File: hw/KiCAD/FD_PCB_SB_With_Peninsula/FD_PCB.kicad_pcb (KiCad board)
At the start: 2 copper layers, 251.3 x 143.9 mm, 169 parts, among them J1 Barrel_Jack_Switch, J10 Conn_01x02, J11 Conn_01x02, J12 Conn_01x02, J13 Conn_02x10_Odd_Even, J14 MQ-4 Gas Sensor, J15 MQ-7 Gas Sensor, J16 MQ-138 Gas Sensor, J17 KY-026 Flame Sensor, J18 Conn_01x10, J19 Conn_01x05, J2 Conn_02x12_Odd_Even, J20 HDC3022, J21 Conn_01x08, J22 MiCS-6814, J23 Conn_01x02, J24 Conn_01x02, J25 Conn_01x02, J3 Conn_02x12_Odd_Even, J4 Conn_02x20_Odd_Even, J5 Conn_02x10_Odd_Even, J6 Conn_01x07, J7 Conn_01x02, J8 Conn_01x08, J9 Conn_01x16, M1 Motor_Servo, M2 Motor_Servo, SW1 SW_Push, SW2 SW_Push, SW3 SW_Push, U1 ADS1115IDGS, U2 OPA2350, U3 OPA2350, U4 ADS1115IDGS

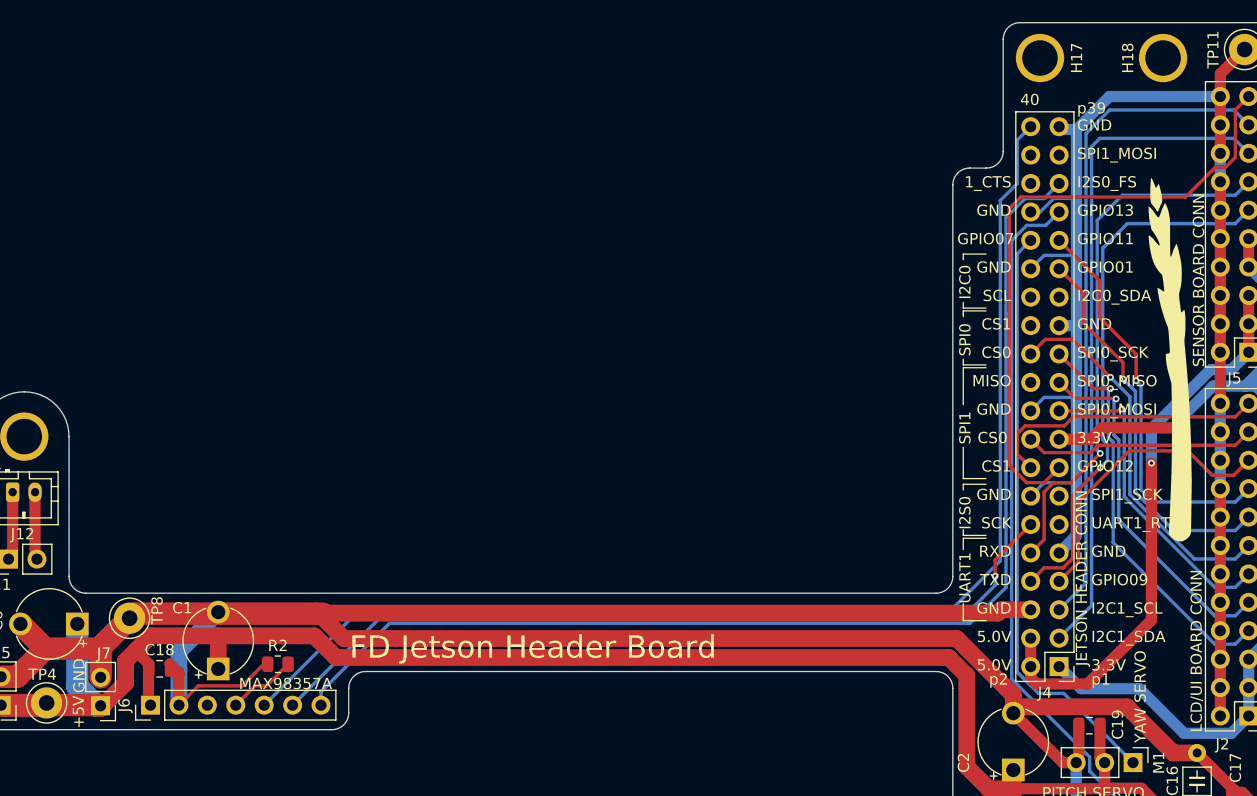
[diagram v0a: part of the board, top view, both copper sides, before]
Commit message: update mounting hole position for H17 and H18
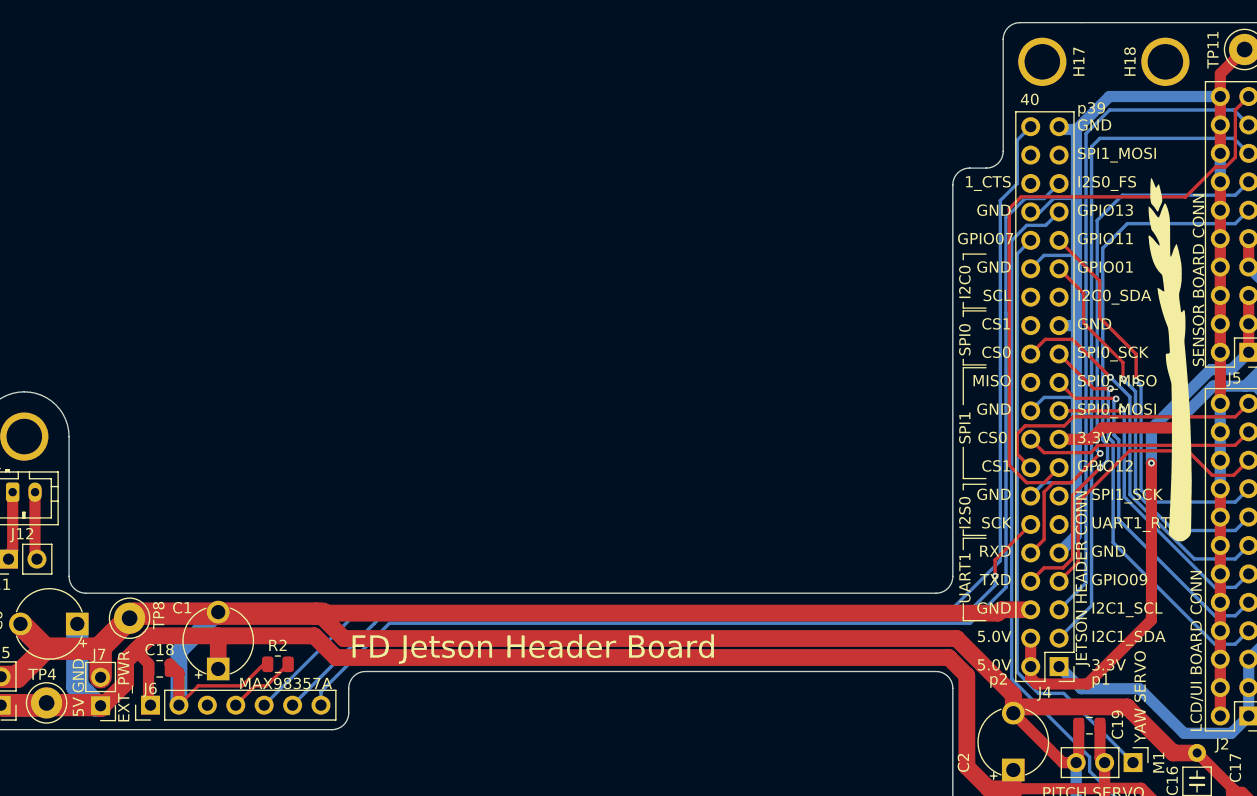
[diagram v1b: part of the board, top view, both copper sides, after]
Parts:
- moved H17 0.40 mm to (114.0, 26.5)
- moved H18 0.40 mm to (125.0, 26.5)
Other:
- board text added: "5V"
- board text added: "EXT_PWR"
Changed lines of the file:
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@@
 	(footprint "ECE445L:MountingHole_4_40"
 		(layer "F.Cu")
-		(at 124.792 26.162)
+		(at 125 26.5)
 		(descr "Mounting Hole 0.125in")
 		(tags "mounting hole 0.125in 4_40")
@@
 		(tags "Through hole pin header THT 1x02 2.54mm single row")
 		(property "Reference" "J7"
-			(at -0.3048 4.6736 0)
+			(at 0.1024 4.5596 0)
 			(layer "F.SilkS")
 			(effects
@@
 		(tags "Through hole pin header THT 1x07 2.54mm single row")
 		(property "Reference" "J6"
-			(at 0 -2.33 90)
+			(at 1.4608 0.0076 180)
 			(layer "F.SilkS")
 			(effects
@@
 		(tags "test point wire loop bead")
 		(property "Reference" "TP8"
-			(at 0.7112 2.4892 90)
+			(at 0.2924 2.6408 90)
 			(layer "F.SilkS")
 			(effects
@@
 	(footprint "ECE445L:MountingHole_4_40"
 		(layer "F.Cu")
-		(at 113.792 26.162)
+		(at 114 26.5)
 		(descr "Mounting Hole 0.125in")
 		(tags "mounting hole 0.125in 4_40")
@@
 		)
 	)
-	(gr_text "+5V"
-		(at 28.448 86.106 90)
-		(layer "F.SilkS" knockout)
+	(gr_text "5V"
+		(at 28.448 85.09 90)
+		(layer "F.SilkS")
 		(effects
 			(font
@@
 	)
 	(gr_text "GND"
-		(at 28.4996 82.944 90)
-		(layer "F.SilkS" knockout)
+		(at 28.448 82.944 90)
+		(layer "F.SilkS")
 		(effects
 			(font
@@
 		)
 	)
+	(gr_text "EXT_PWR"
+		(at 32.512 85.598 90)
+		(layer "F.SilkS" knockout)
+		(effects
+			(font
+				(size 1 1)
+				(thickness 0.1)
+			)
+			(justify left bottom)
+		)
+	)
 	(gr_text "1_CTS"
 		(at 111.252 37.846 0)
@@
 		(layer "Cmts.User")
 		(pts
-			(xy 124.792 26.162) (xy 113.792 26.162)
-		)
-		(height 6.604)
-		(gr_text "11.0000 mm"
-			(at 119.292 18.408 0)
-			(layer "Cmts.User")
-			(effects
-				(font
-					(size 1 1)
-					(thickness 0.15)
-				)
-			)
-		)
-		(format
-			(prefix "")
-			(suffix "")
-			(units 3)
-			(units_format 1)
-			(precision 4)
-		)
-		(style
-			(thickness 0.1)
-			(arrow_length 1.27)
-			(text_position_mode 0)
-			(extension_height 0.58642)
-			(extension_offset 0.5) keep_text_aligned)
-	)
-	(dimension
-		(type aligned)
-		(layer "Cmts.User")
-		(pts
 			(xy 107.5 36) (xy 107.5 74)
 		)
@@
 		(layer "Cmts.User")
 		(pts
-			(xy 19 84.7) (xy 52 84.7)
-		)
-		(height 5.47)
-		(gr_text "33.0000 mm"
-			(at 35.5 89.02 0)
-			(layer "Cmts.User")
-			(effects
-				(font
-					(size 1 1)
-					(thickness 0.15)
-				)
-			)
-		)
-		(format
-			(prefix "")
-			(suffix "")
-			(units 3)
-			(units_format 1)
-			(precision 4)
-		)
-		(style
-			(thickness 0.1)
-			(arrow_length 1.27)
-			(text_position_mode 0)
-			(extension_height 0.58642)
-			(extension_offset 0.5) keep_text_aligned)
-	)
-	(dimension
-		(type aligned)
-		(layer "Cmts.User")
-		(pts
 			(xy 92.675573 105.888) (xy 92.675573 166.878)
 		)
@@
 		(layer "Cmts.User")
 		(pts
-			(xy 52 82.5) (xy 106 82.5)
+			(xy 112 23) (xy 112 36)
 		)
-		(height 7.67)
-		(gr_text "54.0000 mm"
-			(at 79 89.02 0)
+		(height 10.146)
+		(gr_text "13.0000 mm"
+			(at 100.704 29.5 90)
 			(layer "Cmts.User")
 			(effects
@@
 		(layer "Cmts.User")
 		(pts
-			(xy 112 23) (xy 112 36)
+			(xy 125 26.5) (xy 110.5 26.5)
 		)
-		(height 10.146)
-		(gr_text "13.0000 mm"
-			(at 100.704 29.5 90)
+		(height 11.26)
+		(gr_text "14.5000 mm"
+			(at 117.75 14.09 0)
 			(layer "Cmts.User")
 			(effects
@@
 			(layer "Cmts.User")
 			(effects
+				(font
+					(size 1 1)
+					(thickness 0.15)
+				)
+			)
+		)
+		(format
+			(prefix "")
+			(suffix "")
+			(units 3)
+			(units_format 1)
+			(precision 4)
+		)
+		(style
+			(thickness 0.1)
+			(arrow_length 1.27)
+			(text_position_mode 0)
+			(extension_height 0.58642)
+			(extension_offset 0.5) keep_text_aligned)
+	)
+	(dimension
+		(type aligned)
+		(layer "Cmts.User")
+		(pts
+			(xy 125 26.5) (xy 114 26.5)
+		)
+		(height 6.18)
+		(gr_text "11.0000 mm"
+			(at 119.5 19.17 0)
+			(layer "Cmts.User")
+			(effects

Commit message: Decorate Silkscreen
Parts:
- added G***: LOGO, Images:BubblesIcon8, F.Cu at (191.3, 96.0)
- added G***: LOGO, Images:FireAlarmIcon, F.Cu at (58.2, 147.8)
- added G***: LOGO, Images:FireAlarmIcon, B.Cu at (181.1, 84.8)
- added G***: LOGO, Images:FireAlarmIcon, B.Cu at (58.2, 147.8)
- added G***: LOGO, Images:Asparagus-h-stretch, B.Cu at (208.5, 49.3)
- added G***: LOGO, Images:FireIcon, B.Cu at (61.7, 118.1)
- added G***: LOGO, Images:FireIcon, B.Cu at (184.7, 55.1)
- added G***: LOGO, Images:FireIcon, F.Cu at (165.4, 66.5)
- added G***: LOGO, Images:BubblesIcon8, F.Cu at (179.6, 67.1)
- added G***: LOGO, Images:BubblesIcon, F.Cu at (227.8, 54.9)
- added G***: LOGO, Images:BubblesIcon, F.Cu at (206.5, 54.9)
- added G***: LOGO, Images:FireIcon, F.Cu at (166.1, 55.4)
- added G***: LOGO, Images:FireAlarmIconSmall, F.Cu at (28.2, 117.1)
- added G***: LOGO, Images:TempHumIcon, F.Cu at (164.8, 90.9)
- D1: value Red LED -> +5V PWR
- D2: value Green LED -> +3V3 PWR
- D3: value Blue LED -> LED_1
- D4: value Yellow LED -> LED_2
- moved G*** 21.8 mm to (165.9, 45.0), turned to 180 degrees
- moved G*** 0.90 mm to (125.5, 52.6)
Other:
- board text added: "+3V3"
- board text added: "1"
- board text added: "2"
- board text added: "39"
- board text added: "A Purposefully Designed"
- board text added: "A Smart Autonomous Early Fire Detection System"
- board text added: "ADS0_GND"
- board text added: "ADS0_VDD"
- board text added: "ADS1_GND"
- board text added: "ADS1_VDD"
- board text added: "Ain00"
- board text added: "Ain01"
- board text added: "Ain02"
- board text added: "Ain03"
- board text added: "Ain10"
- board text added: "Ain11"
- board text added: "Ain12"
- board text added: "Ain13"
- board text added: "Audio Amp"
- board text added: "BLUE LED"
- board text added: "CH4 Sense"
- board text added: "CO Sense"
- board text added: "CONTROLS"
- board text added: "CS0-0"
- board text added: "CS0-1"
- board text added: "CS1-1"
- board text added: "CTS"
- board text added: "ECE464H SP09 TEAM Michael Chung Anthony Brooks Moby Chiu Raine Salinas Bao Pham"
- board text added: "ECE464H SP09 TEAM Michael Chung Moby Chiu Bao Pham Anthony Brooks Raine Salinas"
- board text added: "FD Barrel Jack Breakout Board"
- board text added: "FD LED BOARD"
- board text added: "FIRE DISTINGUISHER"
- board text added: "GP1"
- board text added: "GP11"
- board text added: "GP9"
- board text added: "GREEN LED"
- board text added: "LCD BOARD CONN"
- board text added: "MG138-AO"
- board text added: "MOSI"
- board text added: "MQ4-AO"
- board text added: "MQ7-AO"
- board text added: "MiCS CO"
- board text added: "MiCS NH3"
- board text added: "MiCS NO2"
- board text added: "NIR Flame Sense"
- board text added: "RED LED"
- board text added: "RTS"
- board text added: "RX"
- board text added: "SB_GND"
- board text added: "SP09 SP26 ECE464H"
- board text added: "SW1"
- board text added: "SW2"
- board text added: "SW3"
- board text added: "Smart Autonomous Early Fire Detection System"
- board text added: "UART1 TX"
- board text added: "UART1_"
- board text added: "VOC Sense"
- board text added: "YELLOW"
- board text added: "ZE07-CO DAC"
- board text removed: "1_CTS"
- board text removed: "UART1_RTS"
- board text removed: "p1"
- board text removed: "p2"
- board text removed: "p39"

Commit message: finalize pcb
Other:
- board text added: "PITCH"
- board text added: "SERVOS"
- board text added: "YAW"
- board text removed: "PITCH SERVO"
- board text removed: "YAW SERVO"
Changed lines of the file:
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@@
 		(at 191.262 96.012)
 		(property "Reference" "G***"
-			(at 0 0 360)
+			(at 0 0 0)
 			(layer "F.SilkS")
 			(hide yes)
@@
 		)
 		(property "Value" "LOGO"
-			(at 0.75 0 360)
+			(at 0.75 0 0)
 			(layer "F.SilkS")
 			(hide yes)
@@
 		)
 		(property "Footprint" "Images:BubblesIcon8"
-			(at 0 0 360)
+			(at 0 0 0)
 			(layer "F.Fab")
 			(hide yes)
@@
 		)
 		(property "Datasheet" ""
-			(at 0 0 360)
+			(at 0 0 0)
 			(layer "F.Fab")
 			(hide yes)
@@
 		)
 		(property "Description" ""
-			(at 0 0 360)
+			(at 0 0 0)
 			(layer "F.Fab")
 			(hide yes)
@@
 		(at 165.354 66.548)
 		(property "Reference" "G***"
-			(at -3.81 -1.524 360)
+			(at -3.81 -1.524 0)
 			(layer "F.SilkS")
 			(hide yes)
@@
 		)
 		(property "Value" "LOGO"
-			(at 0.75 0 360)
+			(at 0.75 0 0)
 			(layer "F.SilkS")
 			(hide yes)
@@
 		)
 		(property "Footprint" "Images:FireIcon"
-			(at 0 0 360)
+			(at 0 0 0)
 			(layer "F.Fab")
 			(hide yes)
@@
 		)
 		(property "Datasheet" ""
-			(at 0 0 360)
+			(at 0 0 0)
 			(layer "F.Fab")
 			(hide yes)
@@
 		)
 		(property "Description" ""
-			(at 0 0 360)
+			(at 0 0 0)
 			(layer "F.Fab")
 			(hide yes)
@@
 		(at 227.838 54.864 180)
 		(property "Reference" "G***"
-			(at 0 0 360)
+			(at 0 0 0)
 			(layer "F.SilkS")
 			(hide yes)
@@
 		)
 		(property "Value" "LOGO"
-			(at 0.75 0 360)
+			(at 0.75 0 0)
 			(layer "F.SilkS")
 			(hide yes)
@@
 		)
 		(property "Footprint" "Images:BubblesIcon"
-			(at 0 0 360)
+			(at 0 0 0)
 			(layer "F.Fab")
 			(hide yes)
@@
 		)
 		(property "Datasheet" ""
-			(at 0 0 360)
+			(at 0 0 0)
 			(layer "F.Fab")
 			(hide yes)
@@
 		)
 		(property "Description" ""
-			(at 0 0 360)
+			(at 0 0 0)
 			(layer "F.Fab")
 			(hide yes)
@@
 		(tags "capacitor")
 		(property "Reference" "C19"
-			(at -2.54 0.1016 90)
+			(at 0.1016 1.5132 180)
 			(layer "F.SilkS")
 			(effects
@@
 		(at 165.862 44.958 180)
 		(property "Reference" "G***"
-			(at -3.81 -1.524 360)
+			(at -3.81 -1.524 0)
 			(layer "F.SilkS")
 			(hide yes)
@@
 		)
 		(property "Value" "LOGO"
-			(at 0.75 0 360)
+			(at 0.75 0 0)
 			(layer "F.SilkS")
 			(hide yes)
@@
 		)
 		(property "Footprint" "Images:FireIcon"
-			(at 0 0 360)
+			(at 0 0 0)
 			(layer "F.Fab")
 			(hide yes)
@@
 		)
 		(property "Datasheet" ""
-			(at 0 0 360)
+			(at 0 0 0)
 			(layer "F.Fab")
 			(hide yes)
@@
 		)
 		(property "Description" ""
-			(at 0 0 360)
+			(at 0 0 0)
 			(layer "F.Fab")
 			(hide yes)
@@
 		(tags "Through hole pin header THT 1x02 2.54mm single row")
 		(property "Reference" "J10"
-			(at -0.0124 4.876 90)
+			(at -2.2968 2.418 180)
 			(layer "F.SilkS")
 			(effects
@@
 		(layer "F.SilkS")
 	)
+	(gr_poly
+		(pts
+			(xy 123.438 87.8132) (xy 124.0028 87.8132) (xy 123.4748 88.392) (xy 123.444 88.392) (xy 123.438 88.386)
+		)
+		(stroke
+			(width 0.1)
+			(type solid)
+		)
+		(fill solid)
+		(layer "F.SilkS")
+	)
 	(gr_line
 		(start 33.437806 156.840233)
@@
 		)
 	)
+	(gr_text "SERVOS"
+		(at 119.126 92.202 0)
+		(layer "F.SilkS")
+		(effects
+			(font
+				(size 1 1)
+				(thickness 0.1)
+			)
+			(justify left bottom)
+		)
+	)
 	(gr_text "CS1"
 		(at 111.252 50.546 0)
@@
 		)
 	)
-	(gr_text "PITCH SERVO"
-		(at 113.964 92.4576 0)
+	(gr_text "YAW"
+		(at 115.698 92.4632 0)
 		(layer "F.SilkS" knockout)
 		(effects
@@
 		)
 	)
-	(gr_text "YAW SERVO"
-		(at 123.362 87.3776 90)
+	(gr_text "PITCH"
+		(at 119.7864 87.7824 0)
 		(layer "F.SilkS" knockout)
 		(effects
@@
 	)
 	(gr_text "SEN0219 CONN"
-		(at 137.3124 99.8728 90)
+		(at 133.35 99.822 90)
 		(layer "F.SilkS" knockout)
 		(effects

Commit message: separate boards and generate pcb production gerber files
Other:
- board text added: "SB_ GND"
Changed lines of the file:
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@@
 		)
 	)
-	(gr_text "SB_GND"
-		(at 208.026 82.804 0)
+	(gr_text "SB_\nGND"
+		(at 208.0768 84.074 0)
 		(layer "B.SilkS")
 		(effects
